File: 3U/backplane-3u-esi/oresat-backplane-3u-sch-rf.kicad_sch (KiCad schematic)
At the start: 6 parts

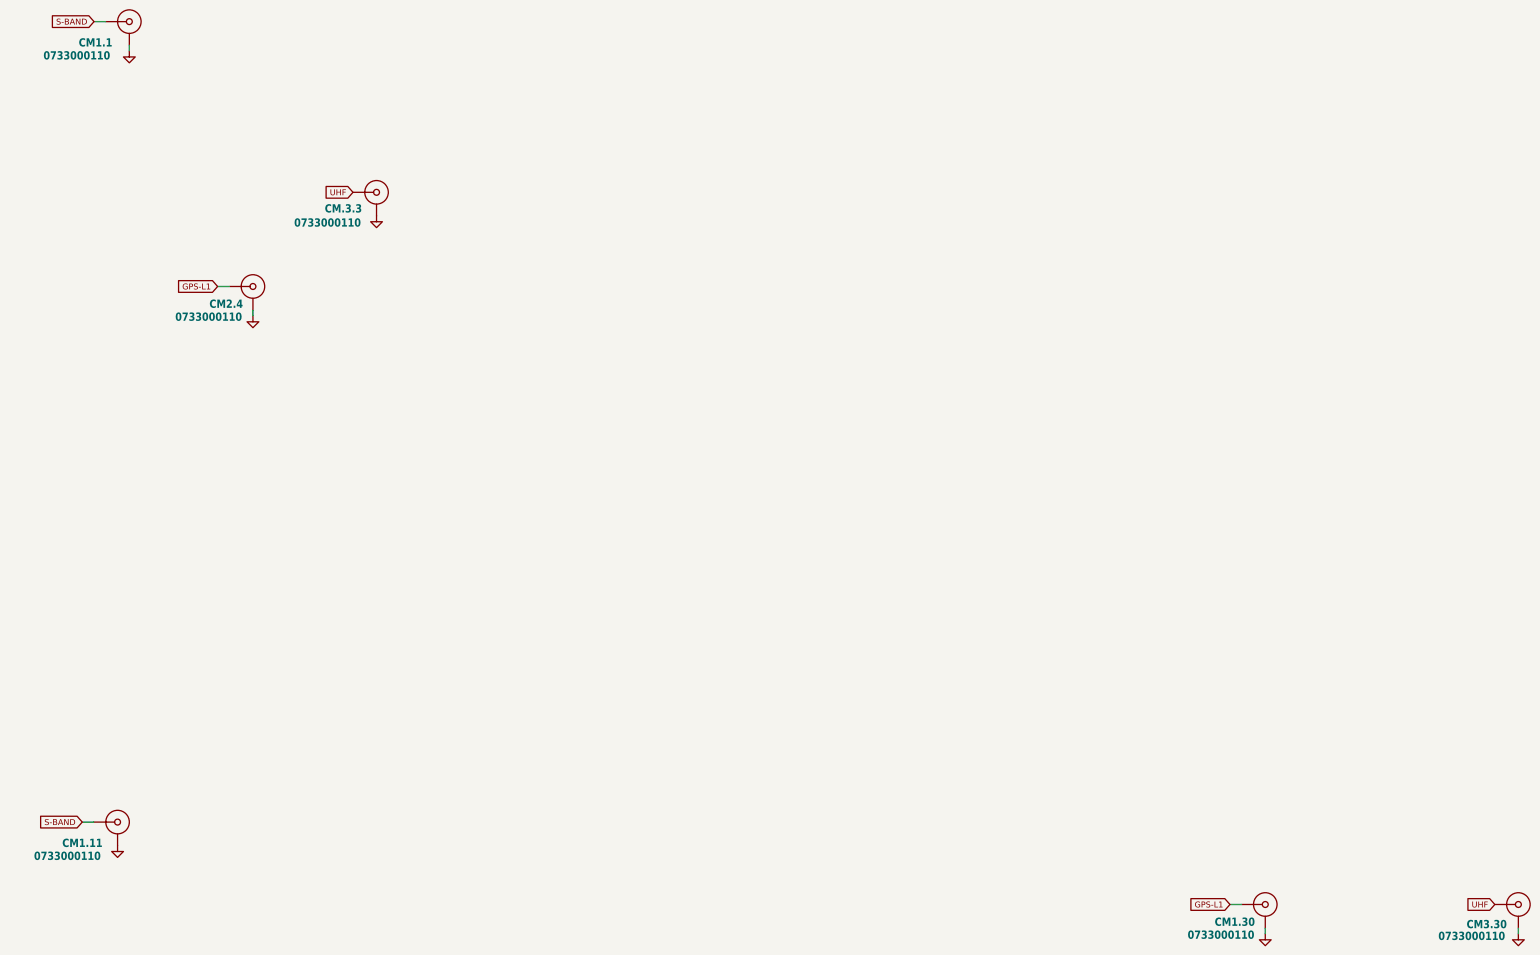
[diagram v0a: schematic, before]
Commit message: Final polishing of ESI backplane and updated Makefile
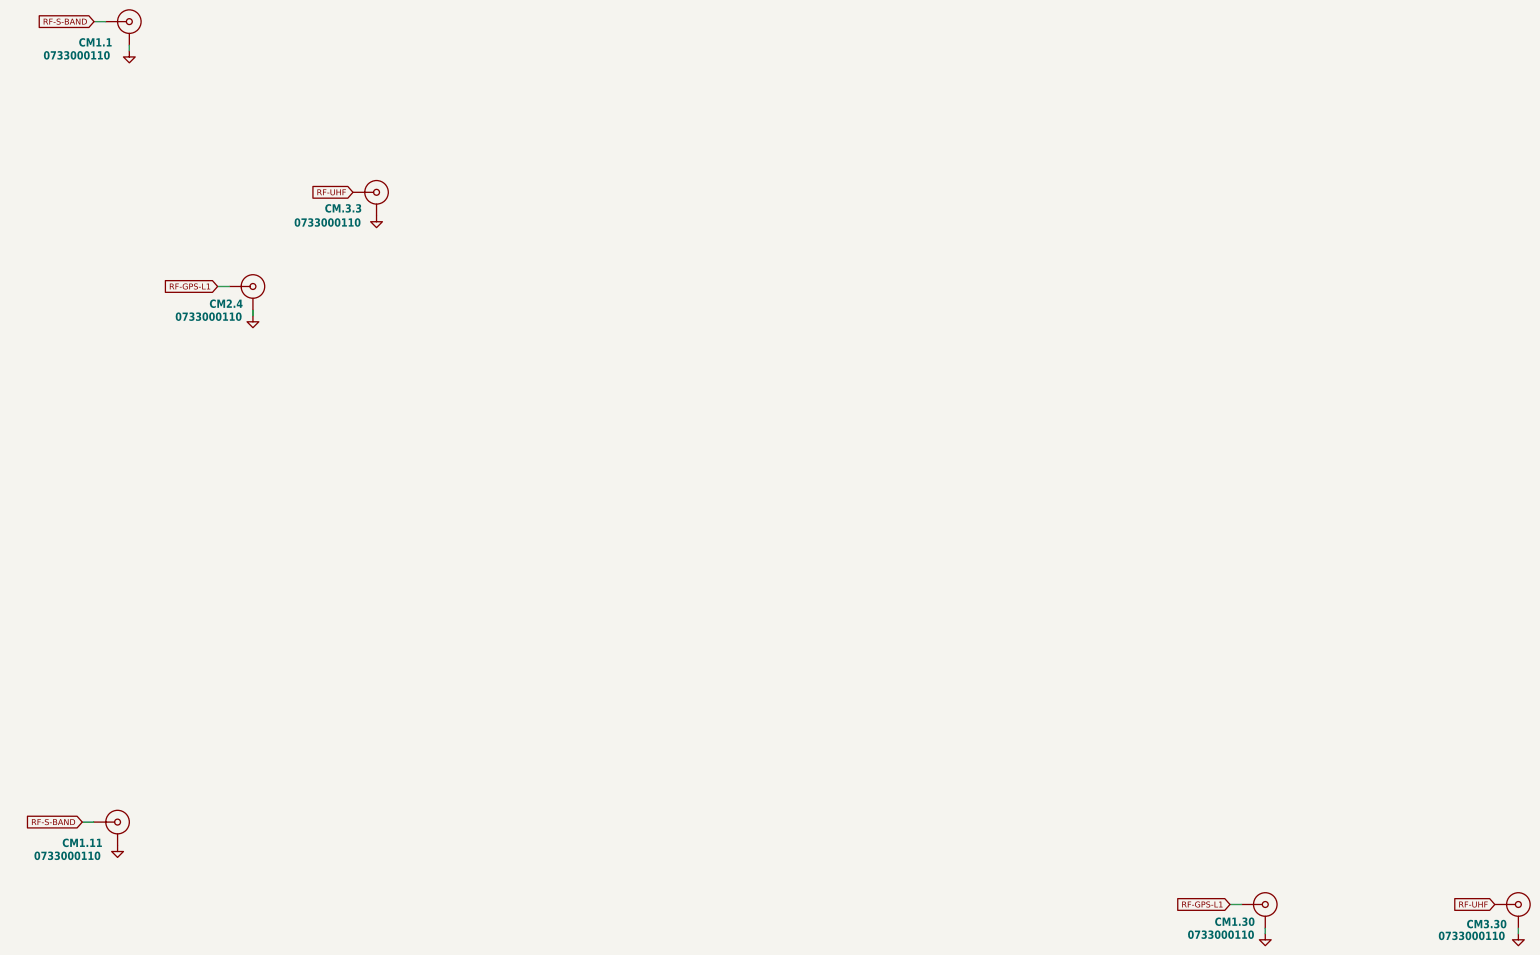
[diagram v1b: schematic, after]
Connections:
- net GPS-L1 renamed RF-GPS-L1
- net S-BAND renamed RF-S-BAND
- net UHF renamed RF-UHF
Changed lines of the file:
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@@
 		)
 	)
-	(global_label "GPS-L1"
+	(global_label "RF-GPS-L1"
 		(shape input)
 		(at 106.68 96.52 180)
@@
 		)
 		(property "Intersheetrefs" "${INTERSHEET_REFS}"
-			(at 96.1353 96.52 0)
+			(at 92.2043 96.52 0)
 			(effects
 				(font
@@
 		)
 	)
-	(global_label "UHF"
+	(global_label "RF-UHF"
 		(shape input)
 		(at 135.89 76.2 180)
@@
 		)
 		(property "Intersheetrefs" "${INTERSHEET_REFS}"
-			(at 129.1552 76.2 0)
+			(at 125.2242 76.2 0)
 			(effects
 				(font
@@
 		)
 	)
-	(global_label "S-BAND"
+	(global_label "RF-S-BAND"
 		(shape input)
 		(at 77.47 212.09 180)
@@
 		)
 		(property "Intersheetrefs" "${INTERSHEET_REFS}"
-			(at 66.7438 212.09 0)
+			(at 62.8128 212.09 0)
 			(effects
 				(font
@@
 		)
 	)
-	(global_label "GPS-L1"
+	(global_label "RF-GPS-L1"
 		(shape input)
 		(at 325.12 229.87 180)
@@
 		)
 		(property "Intersheetrefs" "${INTERSHEET_REFS}"
-			(at 314.5753 229.87 0)
+			(at 310.6443 229.87 0)
 			(effects
 				(font
@@
 		)
 	)
-	(global_label "S-BAND"
+	(global_label "RF-S-BAND"
 		(shape input)
 		(at 80.01 39.37 180)
@@
 		)
 		(property "Intersheetrefs" "${INTERSHEET_REFS}"
-			(at 69.2838 39.37 0)
+			(at 65.3528 39.37 0)
 			(effects
 				(font
@@
 		)
 	)
-	(global_label "UHF"
+	(global_label "RF-UHF"
 		(shape input)
 		(at 382.27 229.87 180)
@@
 		)
 		(property "Intersheetrefs" "${INTERSHEET_REFS}"
-			(at 375.5352 229.87 0)
+			(at 371.6042 229.87 0)
 			(effects
 				(font
